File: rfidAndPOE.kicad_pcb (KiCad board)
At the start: 4 copper layers, 100 x 50 mm, 126 parts, among them J1 0813-1X1T-57-F, J2 SWD, J3 MCU Port B, J4 MCU Port C, P1 PoE-, P2 PoE+, P3 GND, P4 +5V, P5 +12V, P6 +3V3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

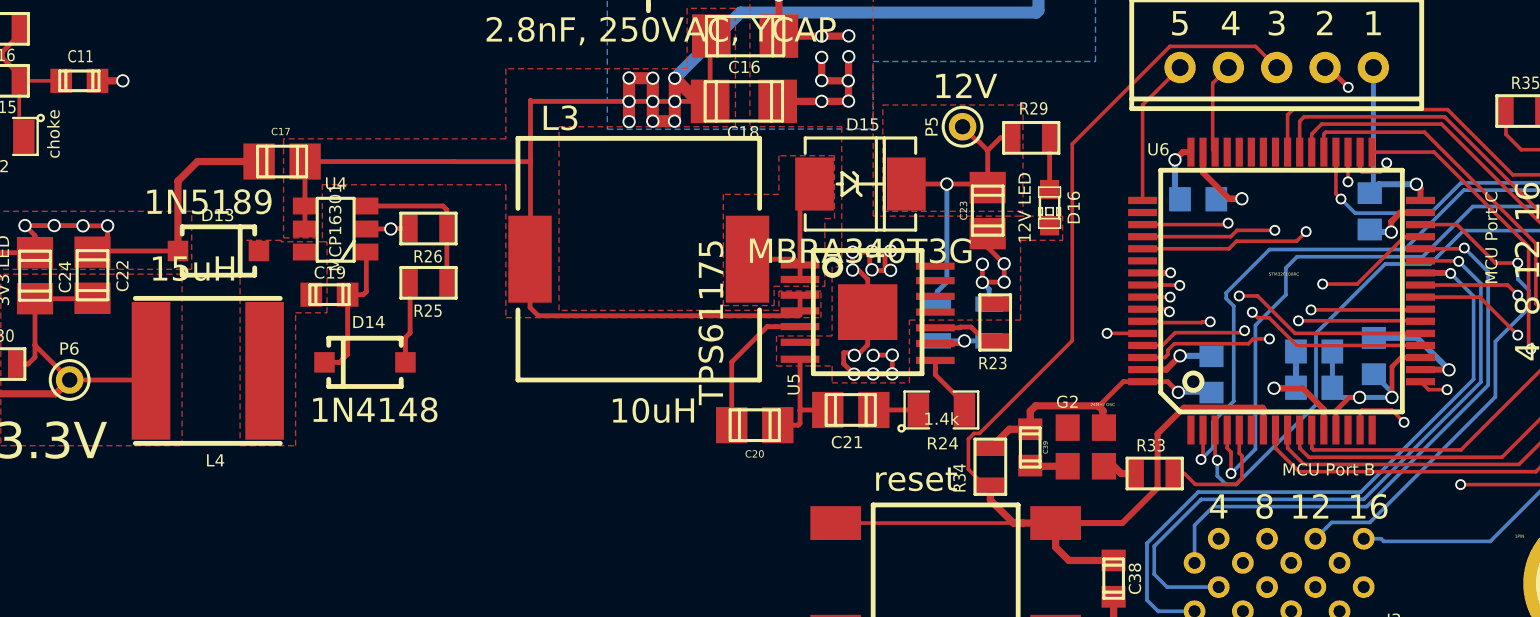
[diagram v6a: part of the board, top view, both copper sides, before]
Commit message: Routed the last traces! Included a preview image of the final pcb.
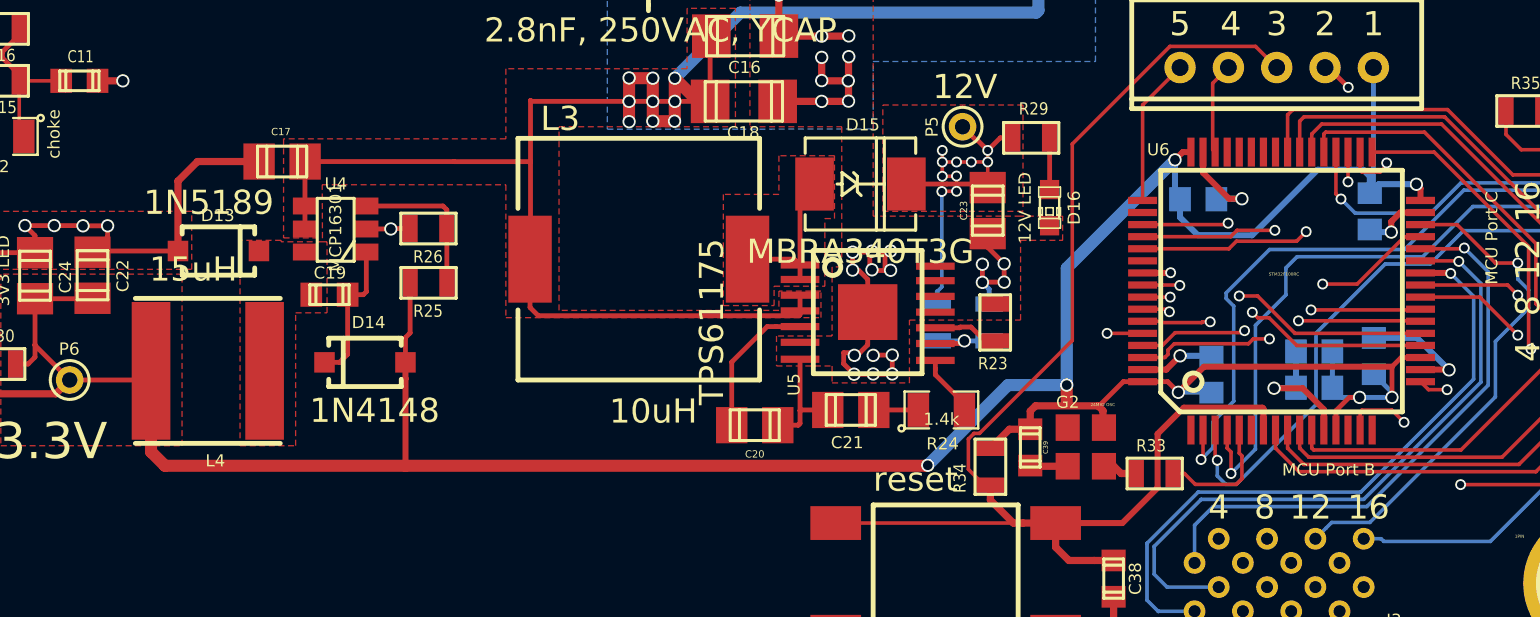
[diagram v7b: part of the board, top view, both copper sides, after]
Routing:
- net 3V3: track 117.6 -> 196.7 mm, vias 9 -> 11
- net 12V: track 12.8 -> 17.2 mm, vias 1 -> 10
- added copper zone on In1.Cu, net 12V
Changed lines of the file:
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@@
     (links 300)
     (no_connects 35)
-    (area 77.749999 30.649999 177.850001 80.750001)
+    (area 72.849999 30.2 177.978572 80.750001)
     (thickness 1.6)
     (drawings 10)
-    (tracks 1400)
+    (tracks 1445)
     (zones 0)
     (modules 126)
@@
     (0 F.Cu signal)
     (1 In1.Cu mixed)
-    (2 In2.Cu signal)
+    (2 In2.Cu signal hide)
     (31 B.Cu signal)
     (32 B.Adhes user)
@@
   )
   (setup
-    (last_trace_width 0.15)
+    (last_trace_width 0.25)
     (user_trace_width 0.15)
     (user_trace_width 0.2)
@@
       (outputformat 1)
       (mirror false)
-      (drillshape 1)
+      (drillshape 0)
       (scaleselection 1)
       (outputdirectory ""))
@@
   (segment (start 139.773427 65.970421) (end 140.773427 65.970421) (width 0.2) (layer F.Cu) (net 18))
   (segment (start 143.825927 69.420421) (end 145.670927 69.420421) (width 0.2) (layer F.Cu) (net 19))
+  (segment (start 114.493766 71.73) (end 124.446375 71.73) (width 0.5) (layer F.Cu) (net 20))
+  (segment (start 124.446375 71.73) (end 146.04 71.73) (width 0.5) (layer F.Cu) (net 20))
+  (segment (start 124.445 68.125) (end 124.446375 68.126375) (width 0.25) (layer F.Cu) (net 20))
+  (segment (start 124.445 67.45) (end 124.445 68.125) (width 0.25) (layer F.Cu) (net 20))
+  (segment (start 124.446375 68.126375) (end 124.446375 71.73) (width 0.25) (layer F.Cu) (net 20))
+  (segment (start 156.49816 60.7) (end 156.49816 61.45038) (width 0.25) (layer B.Cu) (net 20))
+  (segment (start 156.49816 61.45038) (end 157.237781 62.190001) (width 0.25) (layer B.Cu) (net 20))
+  (segment (start 157.237781 62.190001) (end 159.479997 62.190001) (width 0.25) (layer B.Cu) (net 20))
+  (segment (start 159.479997 62.190001) (end 162.189999 59.479999) (width 0.25) (layer B.Cu) (net 20))
+  (segment (start 162.189999 59.479999) (end 164.081419 59.479999) (width 0.25) (layer B.Cu) (net 20))
+  (segment (start 164.081419 59.479999) (end 164.35 59.74858) (width 0.25) (layer B.Cu) (net 20))
+  (segment (start 164.35 59.74858) (end 164.35 60.44816) (width 0.25) (layer B.Cu) (net 20))
+  (segment (start 151.81 68.39) (end 151.81 63.55) (width 0.5) (layer B.Cu) (net 20))
+  (segment (start 151.81 63.55) (end 156.29 59.07) (width 0.5) (layer B.Cu) (net 20))
+  (segment (start 165.27 67.63) (end 157.49 67.63) (width 0.25) (layer F.Cu) (net 20))
+  (segment (start 157.49 67.63) (end 156.43 68.69) (width 0.25) (layer F.Cu) (net 20))
+  (segment (start 151.81 68.39) (end 151.81 69.07) (width 0.5) (layer F.Cu) (net 20))
+  (segment (start 146.06 71.71) (end 149.38 68.39) (width 0.5) (layer B.Cu) (net 20))
+  (segment (start 149.38 68.39) (end 151.81 68.39) (width 0.5) (layer B.Cu) (net 20))
+  (via (at 151.81 68.39) (size 0.55) (drill 0.4) (layers F.Cu B.Cu) (net 20))
+  (segment (start 146.04 71.73) (end 146.06 71.71) (width 0.5) (layer F.Cu) (net 20))
+  (via (at 146.06 71.71) (size 0.55) (drill 0.4) (layers F.Cu B.Cu) (net 20))
+  (segment (start 113.916055 67.802289) (end 113.916055 71.152289) (width 0.5) (layer F.Cu) (net 20))
+  (segment (start 113.916055 71.152289) (end 114.493766 71.73) (width 0.5) (layer F.Cu) (net 20))
   (segment (start 164.5 55.25) (end 164.5 60.29816) (width 0.2) (layer B.Cu) (net 20))
   (segment (start 164.5 60.29816) (end 164.35 60.44816) (width 0.2) (layer B.Cu) (net 20))
@@
   (segment (start 86.699999 59.499999) (end 87.5 60.3) (width 0.2) (layer B.Cu) (net 20))
   (segment (start 87.5 60.3) (end 87.55 60.3) (width 0.2) (layer B.Cu) (net 20))
+  (segment (start 146.45 64.5205) (end 146.64 64.3305) (width 0.15) (layer B.Cu) (net 21))
+  (segment (start 146.64 64.3305) (end 146.64 60.38) (width 0.15) (layer B.Cu) (net 21))
+  (segment (start 147.25 60.37) (end 146.65 60.37) (width 0.15) (layer F.Cu) (net 21))
+  (segment (start 146.65 60.37) (end 146.64 60.38) (width 0.15) (layer F.Cu) (net 21))
+  (via (at 146.64 60.38) (size 0.45) (drill 0.3) (layers F.Cu B.Cu) (net 21))
+  (segment (start 147.25 59.74) (end 147.25 60.37) (width 0.15) (layer F.Cu) (net 21))
+  (via (at 147.25 60.37) (size 0.45) (drill 0.3) (layers F.Cu B.Cu) (net 21))
+  (segment (start 146.66 59.75) (end 147.24 59.75) (width 0.15) (layer F.Cu) (net 21))
+  (segment (start 147.24 59.75) (end 147.25 59.74) (width 0.15) (layer F.Cu) (net 21))
+  (via (at 147.25 59.74) (size 0.45) (drill 0.3) (layers F.Cu B.Cu) (net 21))
+  (segment (start 146.66 59.16) (end 146.66 59.75) (width 0.15) (layer F.Cu) (net 21))
+  (via (at 146.66 59.75) (size 0.45) (drill 0.3) (layers F.Cu B.Cu) (net 21))
+  (segment (start 146.66 59.16) (end 146.66 58.68) (width 0.15) (layer F.Cu) (net 21))
+  (via (at 146.66 58.68) (size 0.45) (drill 0.3) (layers F.Cu B.Cu) (net 21))
+  (segment (start 147.25 59.16) (end 146.66 59.16) (width 0.15) (layer F.Cu) (net 21))
+  (via (at 146.66 59.16) (size 0.45) (drill 0.3) (layers F.Cu B.Cu) (net 21))
+  (segment (start 147.86 59.16) (end 147.25 59.16) (width 0.15) (layer F.Cu) (net 21))
+  (via (at 147.25 59.16) (size 0.45) (drill 0.3) (layers F.Cu B.Cu) (net 21))
+  (segment (start 148.54 59.156108) (end 147.863892 59.156108) (width 0.15) (layer F.Cu) (net 21))
+  (segment (start 147.863892 59.156108) (end 147.86 59.16) (width 0.15) (layer F.Cu) (net 21))
+  (via (at 147.86 59.16) (size 0.45) (drill 0.3) (layers F.Cu B.Cu) (net 21))
+  (segment (start 148.54 59.156108) (end 148.54 58.6805) (width 0.15) (layer F.Cu) (net 21))
+  (via (at 148.54 58.6805) (size 0.45) (drill 0.3) (layers F.Cu B.Cu) (net 21))
+  (segment (start 148.54 60.2175) (end 148.54 59.156108) (width 0.15) (layer F.Cu) (net 21))
+  (via (at 148.54 59.156108) (size 0.45) (drill 0.3) (layers F.Cu B.Cu) (net 21))
   (segment (start 147.5 57.7) (end 148.071499 58.271499) (width 0.2) (layer F.Cu) (net 21))
   (segment (start 148.071499 58.271499) (end 148.130999 58.271499) (width 0.2) (layer F.Cu) (net 21))
   (segment (start 148.130999 58.271499) (end 148.54 58.6805) (width 0.2) (layer F.Cu) (net 21))
-  (segment (start 148.54 60.2175) (end 148.54 58.6805) (width 0.2) (layer F.Cu) (net 21))
   (segment (start 148.54 58.6805) (end 149.0605 58.16) (width 0.2) (layer F.Cu) (net 21))
   (segment (start 149.0605 58.16) (end 149.578 58.16) (width 0.2) (layer F.Cu) (net 21))
@@
   (segment (start 145.173768 60.07) (end 145.173347 60.070421) (width 0.2) (layer F.Cu) (net 21))
   (segment (start 146.45 65.038) (end 146.45 64.5205) (width 0.2) (layer B.Cu) (net 21))
-  (segment (start 146.45 64.5205) (end 146.85 64.1205) (width 0.2) (layer B.Cu) (net 21))
-  (via (at 146.85 60.07) (size 0.55) (drill 0.4) (layers F.Cu B.Cu) (net 21))
-  (segment (start 146.85 64.1205) (end 146.85 60.07) (width 0.2) (layer B.Cu) (net 21))
   (segment (start 87.359 49.244) (end 86.0975 47.9825) (width 0.35) (layer B.Cu) (net 22))
   (segment (start 86.0975 47.9825) (end 86.0975 47.15) (width 0.35) (layer B.Cu) (net 22))
@@
       )
     )
+  )
+  (zone (net 21) (net_name 12V) (layer In1.Cu) (hatch full 0.508)
+    (connect_pads yes (clearance 0.2))
+    (min_thickness 0.2)
+    (fill yes (arc_segments 16) (thermal_gap 0.2) (thermal_bridge_width 0.508))
+    (polygon
+      (pts
+        (xy 146.1 61.2) (xy 146.1 48.6) (xy 146.1 47.7) (xy 173.9 47.7) (xy 173.9 50.4)
+        (xy 150 50.4) (xy 150 61.2)
+      )
+    )
